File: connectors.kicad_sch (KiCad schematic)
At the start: 4 parts, among them J1 Conn_01x04_Pin, J2 Conn_01x04_Pin, J3 Conn_01x09_Pin, J4 Conn_02x03_Odd_Even

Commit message: assigned footprints and added libraries
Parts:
- J1, J2: footprint (none) -> Connector_PinHeader_2.54mm:PinHeader_1x04_P2.54mm_Vertical
- J3: footprint (none) -> Connector_PinHeader_2.54mm:PinHeader_1x09_P2.54mm_Vertical
- J4: footprint (none) -> Connector_PinHeader_2.54mm:PinHeader_2x03_P2.54mm_Vertical
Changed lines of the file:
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@@
 			)
 		)
-		(property "Footprint" ""
+		(property "Footprint" "Connector_PinHeader_2.54mm:PinHeader_1x09_P2.54mm_Vertical"
 			(at 102.87 118.11 0)
 			(effects
@@
 			)
 		)
-		(property "Footprint" ""
+		(property "Footprint" "Connector_PinHeader_2.54mm:PinHeader_2x03_P2.54mm_Vertical"
 			(at 125.73 115.57 0)
 			(effects
@@
 			)
 		)
-		(property "Footprint" ""
+		(property "Footprint" "Connector_PinHeader_2.54mm:PinHeader_1x04_P2.54mm_Vertical"
 			(at 101.6 90.17 0)
 			(effects
@@
 			)
 		)
-		(property "Footprint" ""
+		(property "Footprint" "Connector_PinHeader_2.54mm:PinHeader_1x04_P2.54mm_Vertical"
 			(at 120.65 90.17 0)
 			(effects

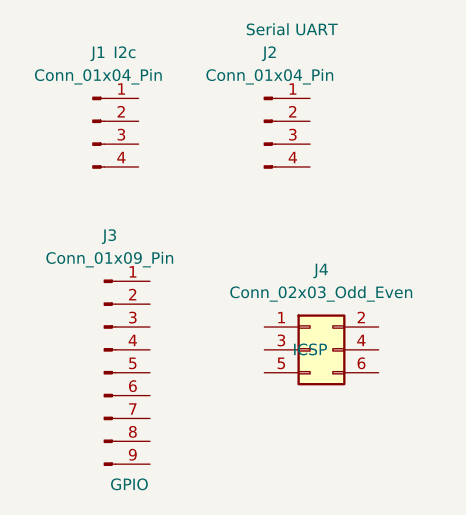
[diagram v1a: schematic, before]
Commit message: wiring for sheet 2 finished  and errors on the main sheet fixed
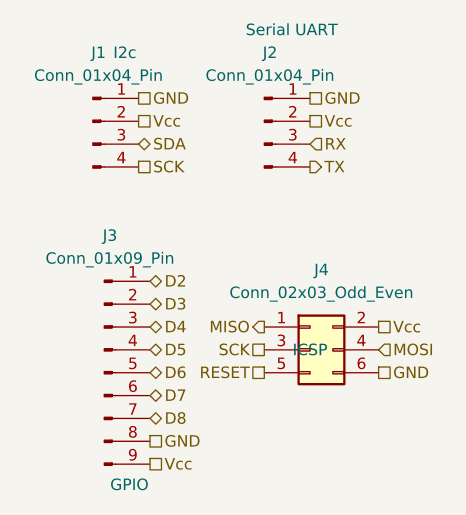
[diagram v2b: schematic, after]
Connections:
- net D2: now reaches J3.1 (Pin_1)
- net D3: now reaches J3.2 (Pin_2)
- net D4: now reaches J3.3 (Pin_3)
- net D5: now reaches J3.4 (Pin_4)
- net D6: now reaches J3.5 (Pin_5)
- net D7: now reaches J3.6 (Pin_6)
- net D8: now reaches J3.7 (Pin_7)
- net GND: now reaches J3.8 (Pin_8)
- net GND: now also J1.1 (Pin_1), J2.1 (Pin_1), J4.6 (Pin_6)
- net Vcc: now reaches J3.9 (Pin_9)
- net Vcc: now also J1.2 (Pin_2), J2.2 (Pin_2), J4.2 (Pin_2)
- net MISO: now reaches J4.1 (Pin_1)
- net SCK: now reaches J4.3 (Pin_3)
- net SCK: now also J1.4 (Pin_4)
- net MOSI: now reaches J4.4 (Pin_4)
- net RESET: now reaches J4.5 (Pin_5)
- net SDA: now reaches J1.3 (Pin_3)
- net RX: now reaches J2.3 (Pin_3)
- net TX: now reaches J2.4 (Pin_4)
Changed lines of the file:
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@@
 	(generator_version "9.0")
 	(paper "A4")
+	(hierarchical_label "D2"
+		(shape bidirectional)
+		(at 107.95 107.95 0)
+		(effects
+			(font
+				(size 1.27 1.27)
+			)
+			(justify left)
+		)
+	)
+	(hierarchical_label "GND"
+		(shape passive)
+		(at 107.95 125.73 0)
+		(effects
+			(font
+				(size 1.27 1.27)
+			)
+			(justify left)
+		)
+	)
+	(hierarchical_label "D7"
+		(shape bidirectional)
+		(at 107.95 120.65 0)
+		(effects
+			(font
+				(size 1.27 1.27)
+			)
+			(justify left)
+		)
+	)
+	(hierarchical_label "RX"
+		(shape input)
+		(at 125.73 92.71 0)
+		(effects
+			(font
+				(size 1.27 1.27)
+			)
+			(justify left)
+		)
+	)
+	(hierarchical_label "D4"
+		(shape bidirectional)
+		(at 107.95 113.03 0)
+		(effects
+			(font
+				(size 1.27 1.27)
+			)
+			(justify left)
+		)
+	)
+	(hierarchical_label "Vcc"
+		(shape passive)
+		(at 133.35 113.03 0)
+		(effects
+			(font
+				(size 1.27 1.27)
+			)
+			(justify left)
+		)
+	)
+	(hierarchical_label "D5"
+		(shape bidirectional)
+		(at 107.95 115.57 0)
+		(effects
+			(font
+				(size 1.27 1.27)
+			)
+			(justify left)
+		)
+	)
+	(hierarchical_label "SCK"
+		(shape passive)
+		(at 106.68 95.25 0)
+		(effects
+			(font
+				(size 1.27 1.27)
+			)
+			(justify left)
+		)
+	)
+	(hierarchical_label "GND"
+		(shape passive)
+		(at 106.68 87.63 0)
+		(effects
+			(font
+				(size 1.27 1.27)
+			)
+			(justify left)
+		)
+	)
+	(hierarchical_label "RESET"
+		(shape passive)
+		(at 120.65 118.11 180)
+		(effects
+			(font
+				(size 1.27 1.27)
+			)
+			(justify right)
+		)
+	)
+	(hierarchical_label "D8"
+		(shape bidirectional)
+		(at 107.95 123.19 0)
+		(effects
+			(font
+				(size 1.27 1.27)
+			)
+			(justify left)
+		)
+	)
+	(hierarchical_label "SDA"
+		(shape bidirectional)
+		(at 106.68 92.71 0)
+		(effects
+			(font
+				(size 1.27 1.27)
+			)
+			(justify left)
+		)
+	)
+	(hierarchical_label "Vcc"
+		(shape passive)
+		(at 106.68 90.17 0)
+		(effects
+			(font
+				(size 1.27 1.27)
+			)
+			(justify left)
+		)
+	)
+	(hierarchical_label "GND"
+		(shape passive)
+		(at 133.35 118.11 0)
+		(effects
+			(font
+				(size 1.27 1.27)
+			)
+			(justify left)
+		)
+	)
+	(hierarchical_label "SCK"
+		(shape passive)
+		(at 120.65 115.57 180)
+		(effects
+			(font
+				(size 1.27 1.27)
+			)
+			(justify right)
+		)
+	)
+	(hierarchical_label "GND"
+		(shape passive)
+		(at 125.73 87.63 0)
+		(effects
+			(font
+				(size 1.27 1.27)
+			)
+			(justify left)
+		)
+	)
+	(hierarchical_label "Vcc"
+		(shape passive)
+		(at 125.73 90.17 0)
+		(effects
+			(font
+				(size 1.27 1.27)
+			)
+			(justify left)
+		)
+	)
+	(hierarchical_label "D3"
+		(shape bidirectional)
+		(at 107.95 110.49 0)
+		(effects
+			(font
+				(size 1.27 1.27)
+			)
+			(justify left)
+		)
+	)
+	(hierarchical_label "MISO"
+		(shape output)
+		(at 120.65 113.03 180)
+		(effects
+			(font
+				(size 1.27 1.27)
+			)
+			(justify right)
+		)
+	)
+	(hierarchical_label "TX"
+		(shape output)
+		(at 125.73 95.25 0)
+		(effects
+			(font
+				(size 1.27 1.27)
+			)
+			(justify left)
+		)
+	)
+	(hierarchical_label "Vcc"
+		(shape passive)
+		(at 107.95 128.27 0)
+		(effects
+			(font
+				(size 1.27 1.27)
+			)
+			(justify left)
+		)
+	)
+	(hierarchical_label "D6"
+		(shape bidirectional)
+		(at 107.95 118.11 0)
+		(effects
+			(font
+				(size 1.27 1.27)
+			)
+			(justify left)
+		)
+	)
+	(hierarchical_label "MOSI"
+		(shape input)
+		(at 133.35 115.57 0)
+		(effects
+			(font
+				(size 1.27 1.27)
+			)
+			(justify left)
+		)
+	)
 	(symbol
 		(lib_id "Connector:Conn_01x09_Pin")

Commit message: fixed references in sheet 2 to match the course material for the purpose of easier wiring during layout design stage
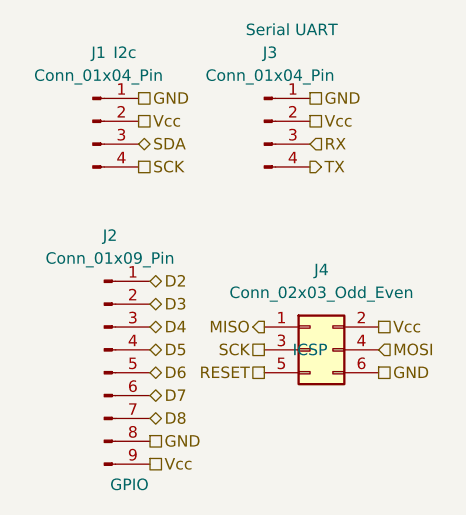
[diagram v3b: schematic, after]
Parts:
- renumbered J3 to J2, J2 to J3
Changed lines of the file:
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@@
 		(on_board yes)
 		(dnp no)
-		(property "Reference" "J3"
+		(property "Reference" "J2"
 			(at 103.505 102.87 0)
 			(effects
@@
 			(project ""
 				(path "/8d241645-05dd-4180-8806-a9efe0716d11/da052fb4-db63-46ba-a21f-c20989841eb3"
-					(reference "J3")
+					(reference "J2")
 					(unit 1)
 				)
@@
 		(on_board yes)
 		(dnp no)
-		(property "Reference" "J2"
+		(property "Reference" "J3"
 			(at 121.285 82.55 0)
 			(effects
@@
 			(project "mcu_data_logger"
 				(path "/8d241645-05dd-4180-8806-a9efe0716d11/da052fb4-db63-46ba-a21f-c20989841eb3"
-					(reference "J2")
+					(reference "J3")
 					(unit 1)
 				)

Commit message: fixed net label bugs for i2c and icsp clock signal ports in the schematics
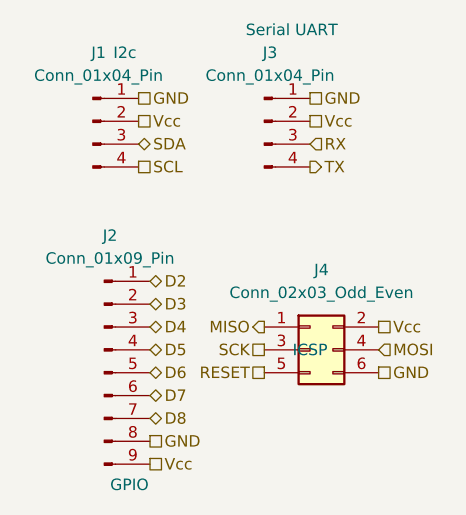
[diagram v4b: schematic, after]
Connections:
- net SCK: no longer J1.4 (Pin_4)
- new net SCL: J1.4 (Pin_4)
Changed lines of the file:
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@@
 		)
 	)
-	(hierarchical_label "SCK"
+	(hierarchical_label "SCL"
 		(shape passive)
 		(at 106.68 95.25 0)
